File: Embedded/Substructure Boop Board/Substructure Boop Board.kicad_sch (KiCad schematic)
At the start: 42 parts, among them U1 PN5321A3HN_C1xx, U2 AD7142ACPZ-500RL7, U3 LD1117S33TR_SOT223, U5 R FFC, Y1 7M-27.120MAAJ-T

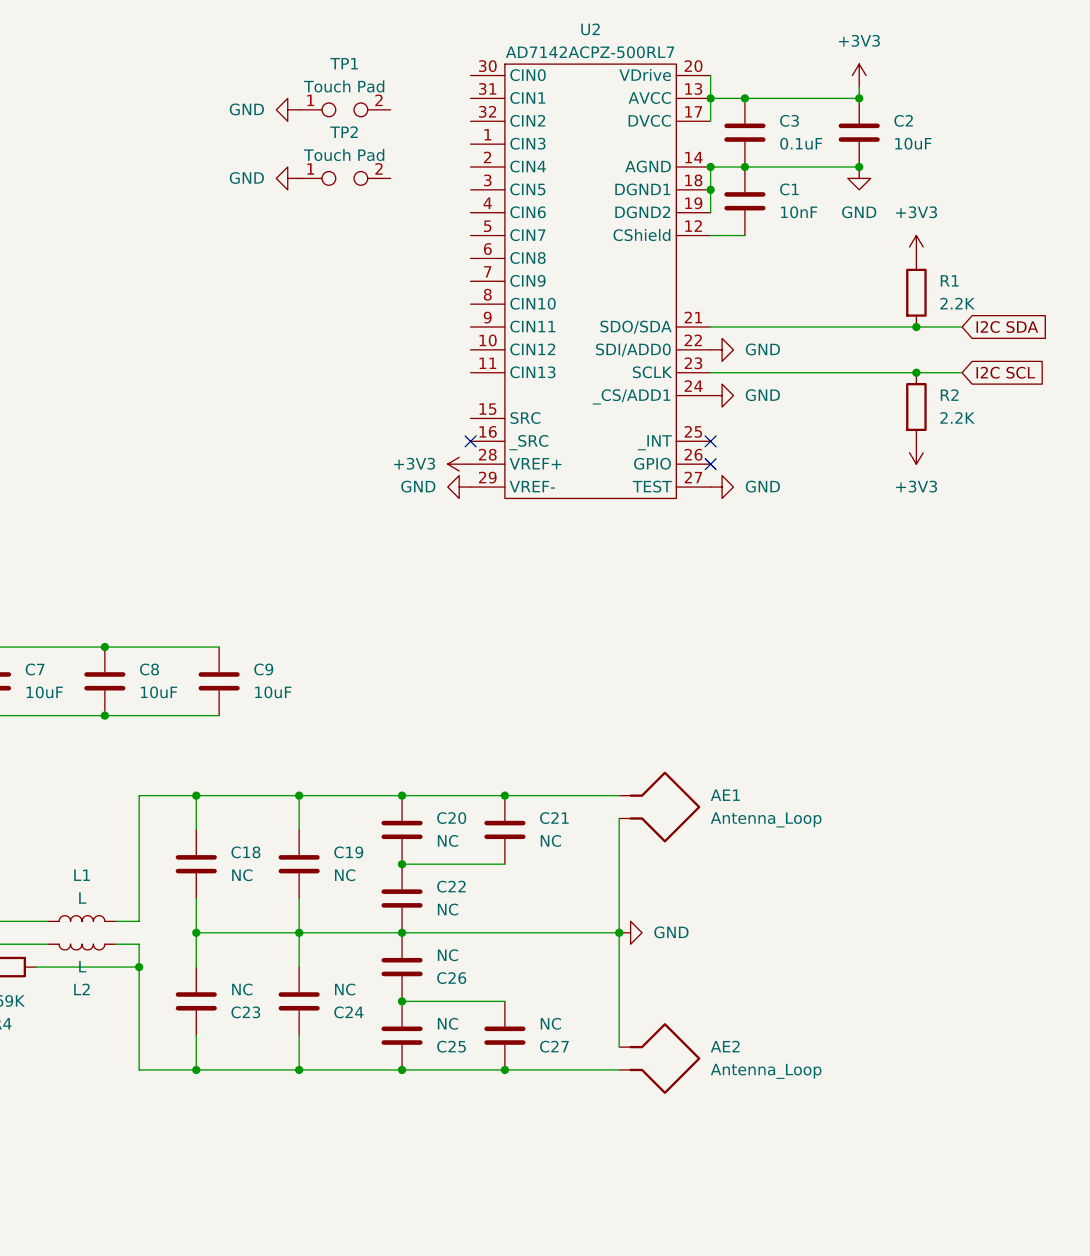
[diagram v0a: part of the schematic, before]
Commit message: Modified Schematic (Added Notes to the Capacitive Pads & Antenna)
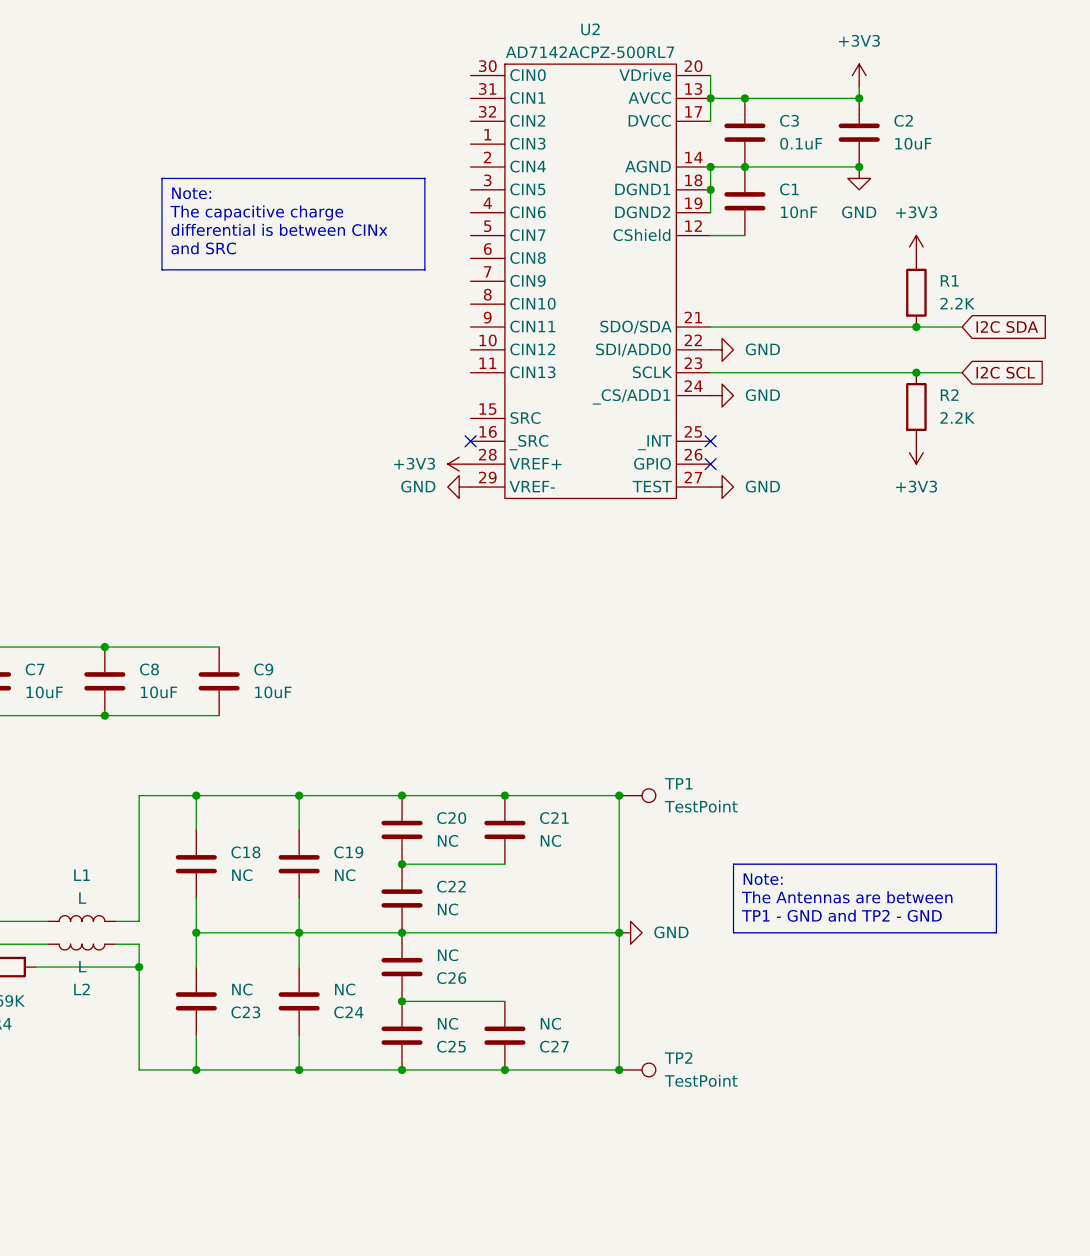
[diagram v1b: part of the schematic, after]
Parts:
- removed AE1, AE2: Antenna_Loop, symbol Device:Antenna_Loop
- removed TP1, TP2: Touch Pad, symbol Connector:TestPoint_2Pole
- added TP1, TP2: TestPoint, TestPoint:TestPoint_Loop_D1.80mm_Drill1.0mm_Beaded, symbol Connector:TestPoint
- L1, L2: footprint (none) -> Inductor_SMD:L_0603_1608Metric_Pad1.05x0.95mm_HandSolder
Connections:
- net GND: now also C18.1, C19.1, C20.1, C21.1, C23.1, C24.1, C25.1, C27.1, L1.2, L2.2, R4.2, TP1.1, TP2.1

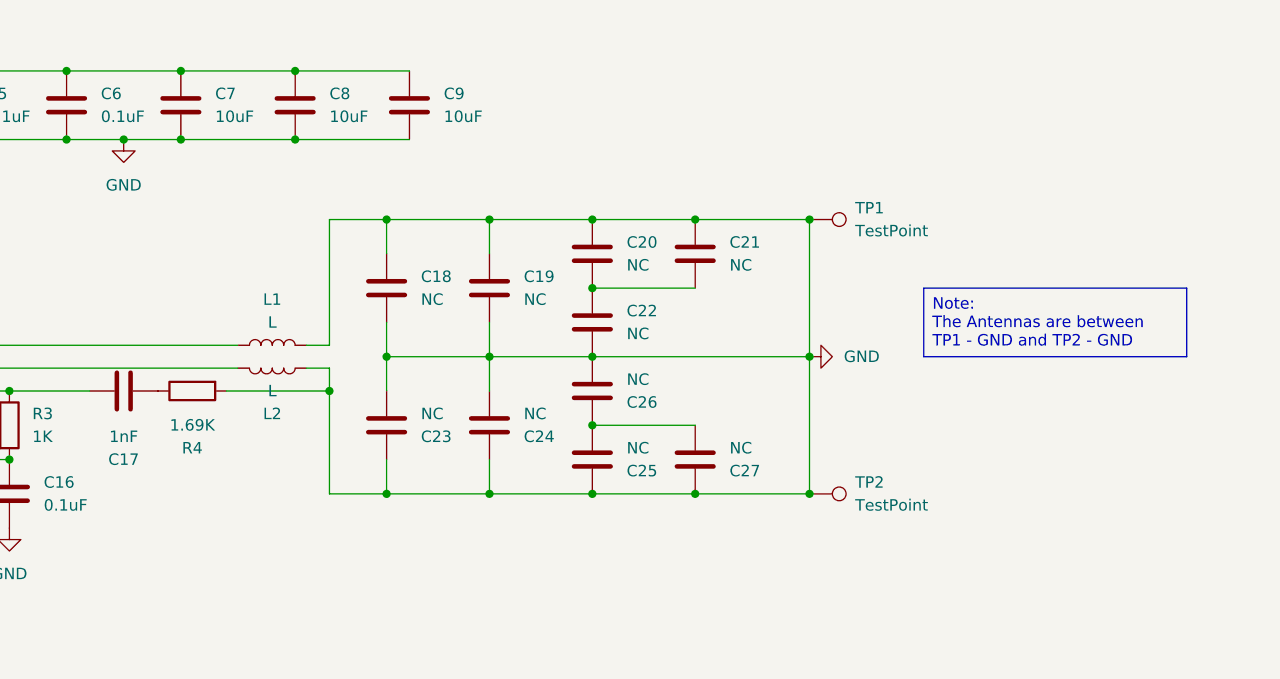
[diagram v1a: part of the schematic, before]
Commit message: Added PCB Antenna Design
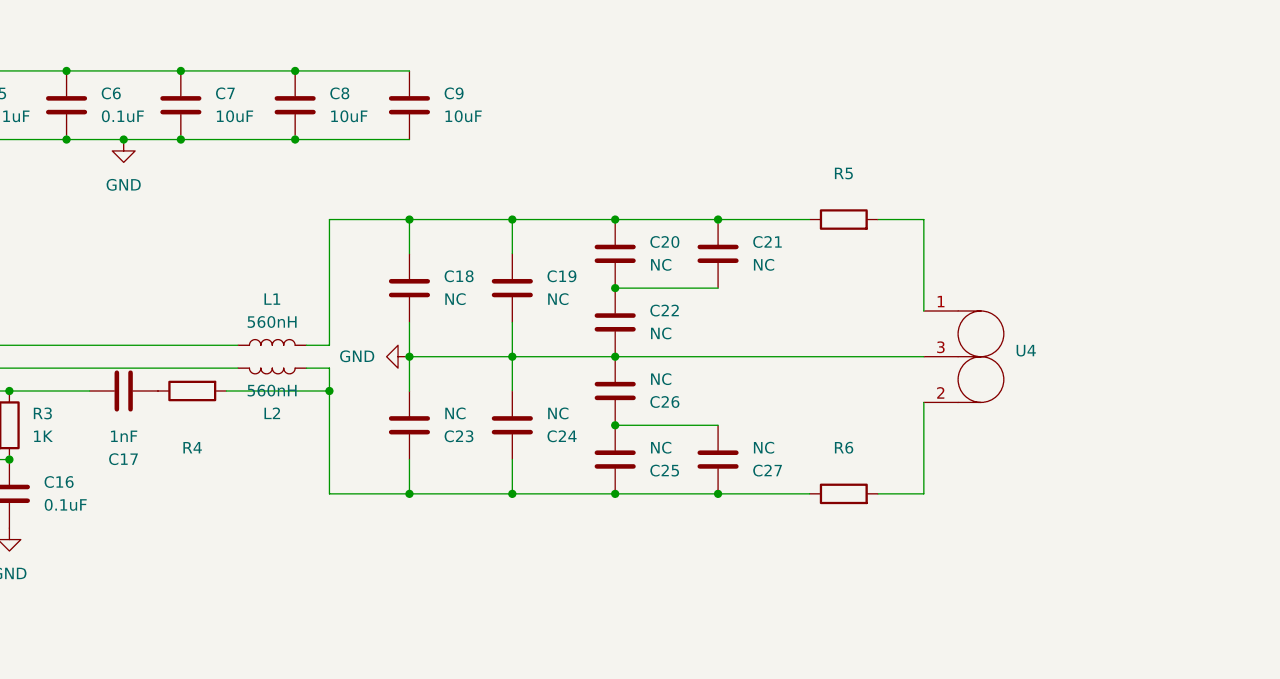
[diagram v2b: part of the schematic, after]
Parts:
- removed TP1, TP2: TestPoint, TestPoint:TestPoint_Loop_D1.80mm_Drill1.0mm_Beaded, symbol Connector:TestPoint
- added R5, R6: ~, Resistor_SMD:R_0603_1608Metric_Pad0.98x0.95mm_HandSolder, symbol Device:R
- added U4: ~, PCB_Antenna:30 x 40 - 2 Pair 2 Layer 2 Turn Loop Antenna, symbol Antenna:2_Loop_Common_Middle_Antenna
- L1, L2: value L -> 560nH
- R4: value 1.69K -> ~
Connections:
- net GND: now also U4.3; no longer C18.1, C19.1, C20.1, C21.1, C23.1, C24.1, C25.1, C27.1, L1.2, L2.2, R4.2
- new net: R5.2, U4.1
- new net: R6.2, U4.2
- new net: C18.1, C19.1, C20.1, C21.1, L1.2, R5.1
- new net: C23.1, C24.1, C25.1, C27.1, L2.2, R4.2, R6.1
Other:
- moved on the sheet: C18, C19, C20, C21, C22, C23, C24, C25, C26, C27

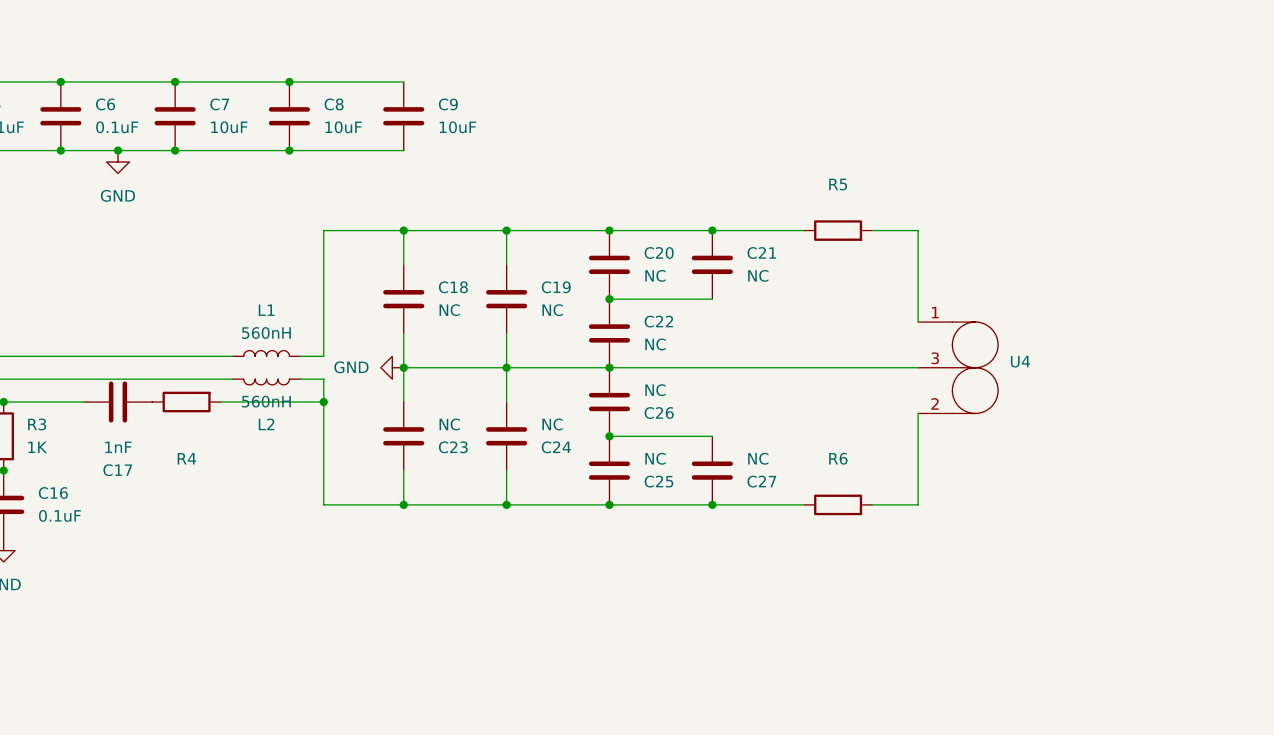
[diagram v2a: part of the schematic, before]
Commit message: Added Antenna LC tank values & EMC filter values
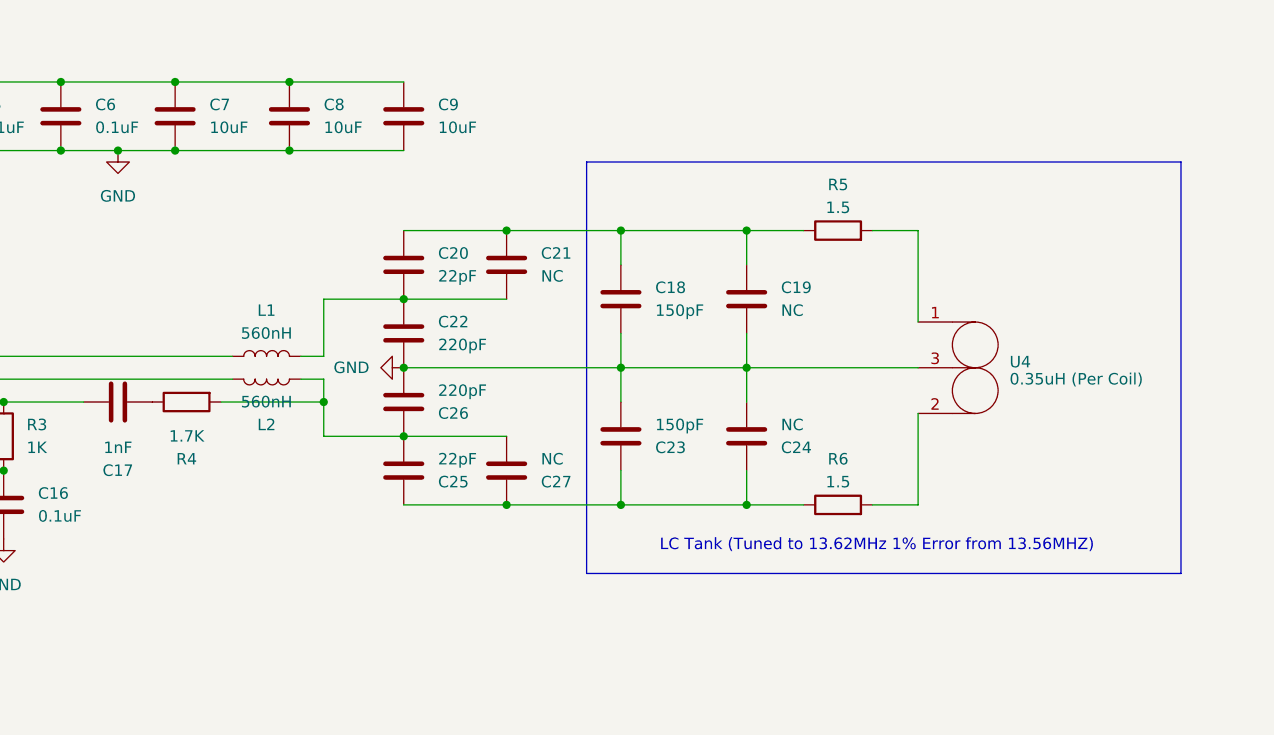
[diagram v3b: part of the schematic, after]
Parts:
- C18, C23: value NC -> 150pF
- C20, C25: value NC -> 22pF
- C22, C26: value NC -> 220pF
- R4: value ~ -> 1.7K
- R5, R6: value ~ -> 1.5
- U4: value ~ -> 0.35uH (Per Coil)
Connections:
- net GND: now also C26.1; no longer C26.2
- net at C18.1, C19.1, C20.1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: no longer L1.2
- net at C20.2, C21.2, C22.1: now also L1.2
- net at C23.1, C24.1, C25.1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: no longer L2.2, R4.2
- net at C25.2, C27.2: now also C26.2, L2.2, R4.2; no longer C26.1
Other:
- note added: "LC Tank (Tuned to 13.62MHz 1% Error from 13.56MHZ)"
- moved on the sheet: C18, C19, C20, C21, C22, C23, C24, C25, C26, C27

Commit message: Added Capacitive sensor component placement
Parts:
- C1, C10, C11, C12, C13, C16, C17, C18, C19, C2, C20, C21, C22, C23, C24, C25, C26, C27, C3, C4, C5, C6, C7, C8, C9: footprint Capacitor_SMD:C_0603_1608Metric_Pad1.08x0.95mm_HandSolder -> Capacitor_SMD:C_0402_1005Metric_Pad0.74x0.62mm_HandSolder
- R1, R2, R3, R4, R5, R6: footprint Resistor_SMD:R_0603_1608Metric_Pad0.98x0.95mm_HandSolder -> Capacitor_SMD:C_0402_1005Metric_Pad0.74x0.62mm_HandSolder
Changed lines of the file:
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@@
 			)
 		)
-		(property "Footprint" "Capacitor_SMD:C_0603_1608Metric_Pad1.08x0.95mm_HandSolder"
+		(property "Footprint" "Capacitor_SMD:C_0402_1005Metric_Pad0.74x0.62mm_HandSolder"
 			(at 147.0152 97.79 0)
 			(effects
@@
 			)
 		)
-		(property "Footprint" "Capacitor_SMD:C_0603_1608Metric_Pad1.08x0.95mm_HandSolder"
+		(property "Footprint" "Capacitor_SMD:C_0402_1005Metric_Pad0.74x0.62mm_HandSolder"
 			(at 134.3152 97.79 0)
 			(effects
@@
 			)
 		)
-		(property "Footprint" "Capacitor_SMD:C_0603_1608Metric_Pad1.08x0.95mm_HandSolder"
+		(property "Footprint" "Capacitor_SMD:C_0402_1005Metric_Pad0.74x0.62mm_HandSolder"
 			(at 172.4152 114.3 0)
 			(effects
@@
 			)
 		)
-		(property "Footprint" "Capacitor_SMD:C_0603_1608Metric_Pad1.08x0.95mm_HandSolder"
+		(property "Footprint" "Capacitor_SMD:C_0402_1005Metric_Pad0.74x0.62mm_HandSolder"
 			(at 32.7152 182.88 0)
 			(effects
@@
 			)
 		)
-		(property "Footprint" "Capacitor_SMD:C_0603_1608Metric_Pad1.08x0.95mm_HandSolder"
+		(property "Footprint" "Capacitor_SMD:C_0402_1005Metric_Pad0.74x0.62mm_HandSolder"
 			(at 64.4652 182.88 0)
 			(effects
@@
 			)
 		)
-		(property "Footprint" "Capacitor_SMD:C_0603_1608Metric_Pad1.08x0.95mm_HandSolder"
+		(property "Footprint" "Capacitor_SMD:C_0402_1005Metric_Pad0.74x0.62mm_HandSolder"
 			(at 210.5152 125.73 0)
 			(effects
@@
 			)
 		)
-		(property "Footprint" "Resistor_SMD:R_0603_1608Metric_Pad0.98x0.95mm_HandSolder"
+		(property "Footprint" "Capacitor_SMD:C_0402_1005Metric_Pad0.74x0.62mm_HandSolder"
 			(at 247.142 50.8 90)
 			(effects
@@
 			)
 		)
-		(property "Footprint" "Capacitor_SMD:C_0603_1608Metric_Pad1.08x0.95mm_HandSolder"
+		(property "Footprint" "Capacitor_SMD:C_0402_1005Metric_Pad0.74x0.62mm_HandSolder"
 			(at 172.4152 121.92 0)
 			(effects
@@
 			)
 		)
-		(property "Footprint" "Capacitor_SMD:C_0603_1608Metric_Pad1.08x0.95mm_HandSolder"
+		(property "Footprint" "Capacitor_SMD:C_0402_1005Metric_Pad0.74x0.62mm_HandSolder"
 			(at 121.6152 97.79 0)
 			(effects
@@
 			)
 		)
-		(property "Footprint" "Capacitor_SMD:C_0603_1608Metric_Pad1.08x0.95mm_HandSolder"
+		(property "Footprint" "Capacitor_SMD:C_0402_1005Metric_Pad0.74x0.62mm_HandSolder"
 			(at 230.8352 44.45 0)
 			(effects
@@
 			)
 		)
-		(property "Footprint" "Capacitor_SMD:C_0603_1608Metric_Pad1.08x0.95mm_HandSolder"
+		(property "Footprint" "Capacitor_SMD:C_0402_1005Metric_Pad0.74x0.62mm_HandSolder"
 			(at 108.9152 97.79 0)
 			(effects
@@
 			)
 		)
-		(property "Footprint" "Capacitor_SMD:C_0603_1608Metric_Pad1.08x0.95mm_HandSolder"
+		(property "Footprint" "Capacitor_SMD:C_0402_1005Metric_Pad0.74x0.62mm_HandSolder"
 			(at 230.8352 36.83 0)
 			(effects
@@
 			)
 		)
-		(property "Footprint" "Capacitor_SMD:C_0603_1608Metric_Pad1.08x0.95mm_HandSolder"
+		(property "Footprint" "Capacitor_SMD:C_0402_1005Metric_Pad0.74x0.62mm_HandSolder"
 			(at 243.5352 36.83 0)
 			(effects
@@
 			)
 		)
-		(property "Footprint" "Resistor_SMD:R_0603_1608Metric_Pad0.98x0.95mm_HandSolder"
+		(property "Footprint" "Capacitor_SMD:C_0402_1005Metric_Pad0.74x0.62mm_HandSolder"
 			(at 219.71 108.458 90)
 			(effects
@@
 			)
 		)
-		(property "Footprint" "Resistor_SMD:R_0603_1608Metric_Pad0.98x0.95mm_HandSolder"
+		(property "Footprint" "Capacitor_SMD:C_0402_1005Metric_Pad0.74x0.62mm_HandSolder"
 			(at 219.71 138.938 90)
 			(effects
@@
 			)
 		)
-		(property "Footprint" "Capacitor_SMD:C_0603_1608Metric_Pad1.08x0.95mm_HandSolder"
+		(property "Footprint" "Capacitor_SMD:C_0402_1005Metric_Pad0.74x0.62mm_HandSolder"
 			(at 210.5152 118.11 0)
 			(effects
@@
 			)
 		)
-		(property "Footprint" "Capacitor_SMD:C_0603_1608Metric_Pad1.08x0.95mm_HandSolder"
+		(property "Footprint" "Capacitor_SMD:C_0402_1005Metric_Pad0.74x0.62mm_HandSolder"
 			(at 159.7152 97.79 0)
 			(effects
@@
 			)
 		)
-		(property "Footprint" "Capacitor_SMD:C_0603_1608Metric_Pad1.08x0.95mm_HandSolder"
+		(property "Footprint" "Capacitor_SMD:C_0402_1005Metric_Pad0.74x0.62mm_HandSolder"
 			(at 183.8452 114.3 0)
 			(effects
@@
 			)
 		)
-		(property "Footprint" "Resistor_SMD:R_0603_1608Metric_Pad0.98x0.95mm_HandSolder"
+		(property "Footprint" "Capacitor_SMD:C_0402_1005Metric_Pad0.74x0.62mm_HandSolder"
 			(at 247.142 63.5 90)
 			(effects
@@
 			)
 		)
-		(property "Footprint" "Capacitor_SMD:C_0603_1608Metric_Pad1.08x0.95mm_HandSolder"
+		(property "Footprint" "Capacitor_SMD:C_0402_1005Metric_Pad0.74x0.62mm_HandSolder"
 			(at 172.4152 97.79 0)
 			(effects
@@
 			)
 		)
-		(property "Footprint" "Capacitor_SMD:C_0603_1608Metric_Pad1.08x0.95mm_HandSolder"
+		(property "Footprint" "Capacitor_SMD:C_0402_1005Metric_Pad0.74x0.62mm_HandSolder"
 			(at 143.51 126.6952 0)
 			(effects
@@
 			)
 		)
-		(property "Footprint" "Capacitor_SMD:C_0603_1608Metric_Pad1.08x0.95mm_HandSolder"
+		(property "Footprint" "Capacitor_SMD:C_0402_1005Metric_Pad0.74x0.62mm_HandSolder"
 			(at 72.0852 93.98 0)
 			(effects
@@
 			)
 		)
-		(property "Footprint" "Capacitor_SMD:C_0603_1608Metric_Pad1.08x0.95mm_HandSolder"
+		(property "Footprint" "Capacitor_SMD:C_0402_1005Metric_Pad0.74x0.62mm_HandSolder"
 			(at 84.7852 93.98 0)
 			(effects
@@
 			)
 		)
-		(property "Footprint" "Capacitor_SMD:C_0603_1608Metric_Pad1.08x0.95mm_HandSolder"
+		(property "Footprint" "Capacitor_SMD:C_0402_1005Metric_Pad0.74x0.62mm_HandSolder"
 			(at 183.8452 129.54 0)
 			(effects
@@
 			)
 		)
-		(property "Footprint" "Capacitor_SMD:C_0603_1608Metric_Pad1.08x0.95mm_HandSolder"
+		(property "Footprint" "Capacitor_SMD:C_0402_1005Metric_Pad0.74x0.62mm_HandSolder"
 			(at 170.4848 129.54 0)
 			(effects
@@
 			)
 		)
-		(property "Footprint" "Capacitor_SMD:C_0603_1608Metric_Pad1.08x0.95mm_HandSolder"
+		(property "Footprint" "Capacitor_SMD:C_0402_1005Metric_Pad0.74x0.62mm_HandSolder"
 			(at 127.9652 140.97 0)
 			(effects
@@
 			)
 		)
-		(property "Footprint" "Capacitor_SMD:C_0603_1608Metric_Pad1.08x0.95mm_HandSolder"
+		(property "Footprint" "Capacitor_SMD:C_0402_1005Metric_Pad0.74x0.62mm_HandSolder"
 			(at 172.4152 129.54 0)
 			(effects
@@
 			)
 		)
-		(property "Footprint" "Capacitor_SMD:C_0603_1608Metric_Pad1.08x0.95mm_HandSolder"
+		(property "Footprint" "Capacitor_SMD:C_0402_1005Metric_Pad0.74x0.62mm_HandSolder"
 			(at 196.5452 125.73 0)
 			(effects
@@
 			)
 		)
-		(property "Footprint" "Capacitor_SMD:C_0603_1608Metric_Pad1.08x0.95mm_HandSolder"
+		(property "Footprint" "Capacitor_SMD:C_0402_1005Metric_Pad0.74x0.62mm_HandSolder"
 			(at 196.5452 118.11 0)
 			(effects
@@
 			)
 		)
-		(property "Footprint" "Resistor_SMD:R_0603_1608Metric_Pad0.98x0.95mm_HandSolder"
+		(property "Footprint" "Capacitor_SMD:C_0402_1005Metric_Pad0.74x0.62mm_HandSolder"
 			(at 125.222 129.54 90)
 			(effects
@@
 			)
 		)
-		(property "Footprint" "Resistor_SMD:R_0603_1608Metric_Pad0.98x0.95mm_HandSolder"
+		(property "Footprint" "Capacitor_SMD:C_0402_1005Metric_Pad0.74x0.62mm_HandSolder"
 			(at 147.32 123.952 90)
 			(effects
